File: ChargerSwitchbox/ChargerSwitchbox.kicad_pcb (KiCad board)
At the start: 2 copper layers, 64.1 x 43.2 mm, 13 parts, among them J1 Charger Control, J2 Charger LV, J3 Charger Current Direct, J4 Estop Connector, J5 Charger Current Out, J6 Connector Interlock, U1 PS2501-1, U2 G2RL-1A-E, U3 G2RL-1A-E

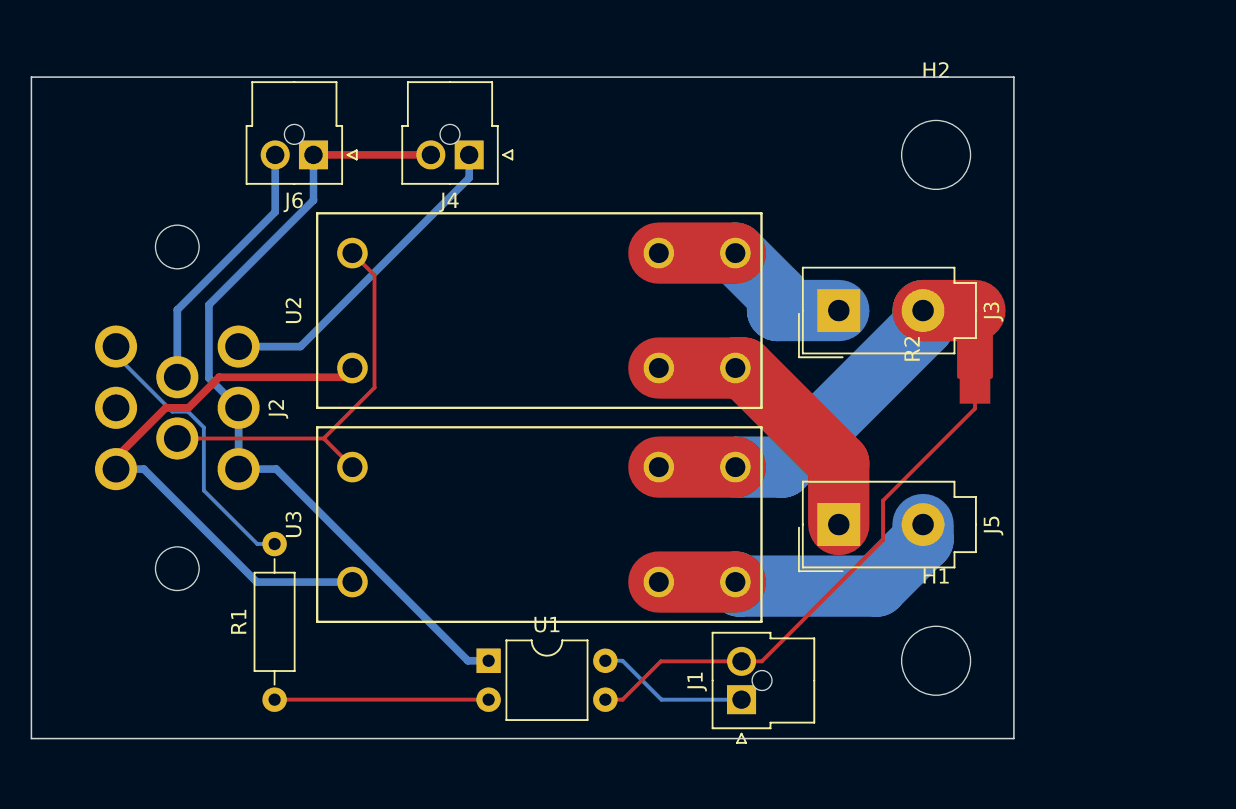
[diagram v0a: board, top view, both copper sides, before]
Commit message: Tweak silkscreen labels on boards for final run
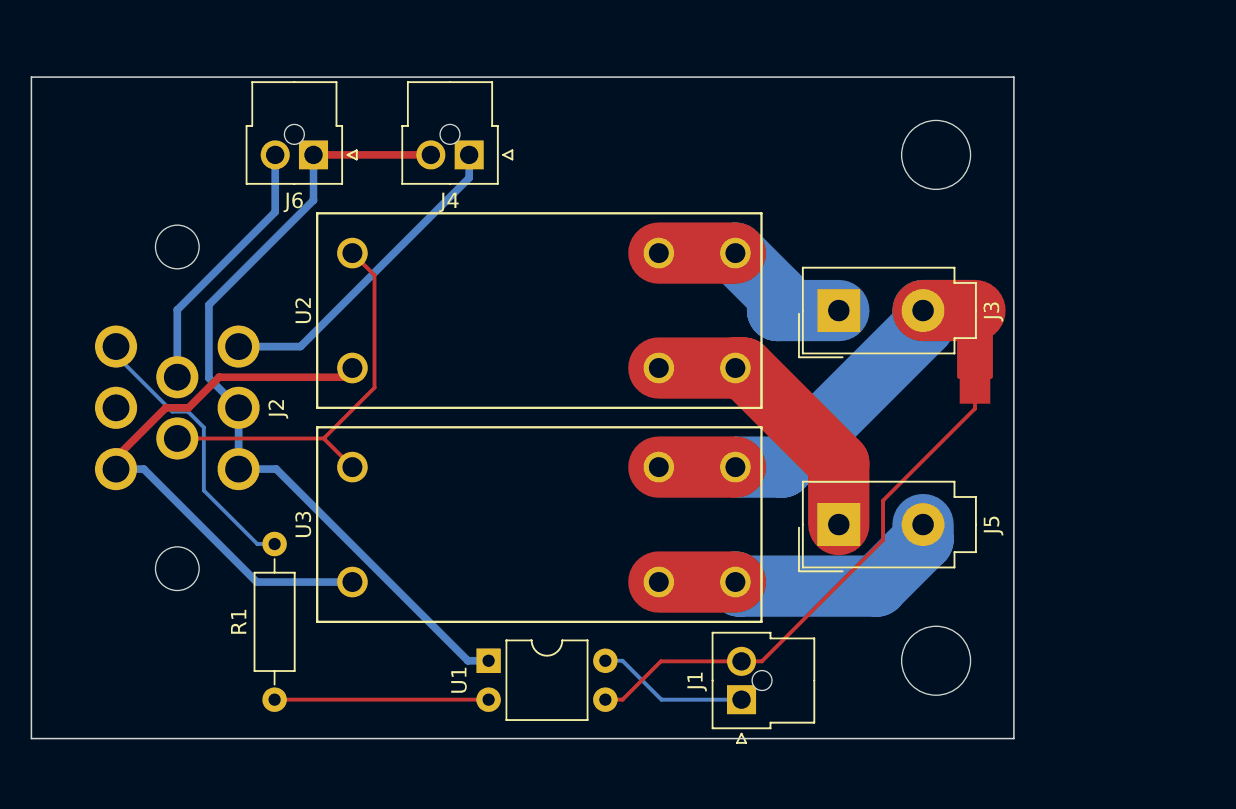
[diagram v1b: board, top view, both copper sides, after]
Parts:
- turned H2 to 180 degrees
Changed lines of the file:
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@@
     (tags "mounting hole 4.5mm no annular")
     (attr virtual)
-    (fp_text reference H1 (at 0 -5.5) (layer F.SilkS)
+    (fp_text reference H1 (at 0 -5.5) (layer F.SilkS) hide
       (effects (font (size 1 1) (thickness 0.15)))
     )
@@
     (descr "Just a \"Net tie\" as an more or less elegant way to connect two different nets without disturbing ERC and DRC.")
     (tags "Just a \"Net tie\" as an more or less elegant way to connect two different nets without disturbing ERC and DRC.")
-    (fp_text reference R2 (at -0.04064 4.06908 270) (layer F.SilkS)
+    (fp_text reference R2 (at 1.905 2.54 270) (layer F.SilkS) hide
       (effects (font (size 1 1) (thickness 0.15)))
     )
@@
     (descr "4-lead though-hole mounted DIP package, row spacing 7.62 mm (300 mils)")
     (tags "THT DIP DIL PDIP 2.54mm 7.62mm 300mil")
-    (fp_text reference U1 (at 3.81 -2.33) (layer F.SilkS)
+    (fp_text reference U1 (at -1.905 1.27 90) (layer F.SilkS)
       (effects (font (size 1 1) (thickness 0.15)))
     )
@@
   (module FSFootprints:G2RL-1A-E (layer F.Cu)
     (at 153.67 43.18)
-    (fp_text reference U2 (at -3.81 0 270) (layer F.SilkS)
+    (fp_text reference U2 (at -3.175 0 270) (layer F.SilkS)
       (effects (font (size 1 1) (thickness 0.15)))
     )
@@
   (module FSFootprints:G2RL-1A-E (layer F.Cu)
     (at 153.67 57.15)
-    (fp_text reference U3 (at -3.81 0 270) (layer F.SilkS)
+    (fp_text reference U3 (at -3.175 0 270) (layer F.SilkS)
       (effects (font (size 1 1) (thickness 0.15)))
     )
@@
   )
   (module Mounting_Holes:MountingHole_4.5mm (layer F.Cu)
-    (at 191.77 33.02)
+    (at 191.77 33.02 180)
     (descr "Mounting Hole 4.5mm, no annular")
     (tags "mounting hole 4.5mm no annular")
     (attr virtual)
-    (fp_text reference H2 (at 0 -5.5) (layer F.SilkS)
+    (fp_text reference H2 (at 0 -5.5 180) (layer F.SilkS) hide
       (effects (font (size 1 1) (thickness 0.15)))
     )
-    (fp_text value MtngHole (at 0 5.5) (layer F.Fab)
+    (fp_text value MtngHole (at 0 5.5 180) (layer F.Fab)
       (effects (font (size 1 1) (thickness 0.15)))
     )
-    (fp_text user %R (at 0.3 0) (layer F.Fab)
+    (fp_text user %R (at 0.3 0 180) (layer F.Fab)
       (effects (font (size 1 1) (thickness 0.15)))
     )
     (fp_circle (center 0 0) (end 4.5 0) (layer Cmts.User) (width 0.15))
     (fp_circle (center 0 0) (end 4.75 0) (layer F.CrtYd) (width 0.05))
-    (pad 1 np_thru_hole circle (at 0 0) (size 4.5 4.5) (drill 4.5) (layers *.Cu *.Mask))
+    (pad 1 np_thru_hole circle (at 0 0 180) (size 4.5 4.5) (drill 4.5) (layers *.Cu *.Mask))
   )
   (module Connectors_Molex:Molex_NanoFit_1x02x2.50mm_Straight (layer F.Cu)

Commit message: Revise boards based on design review
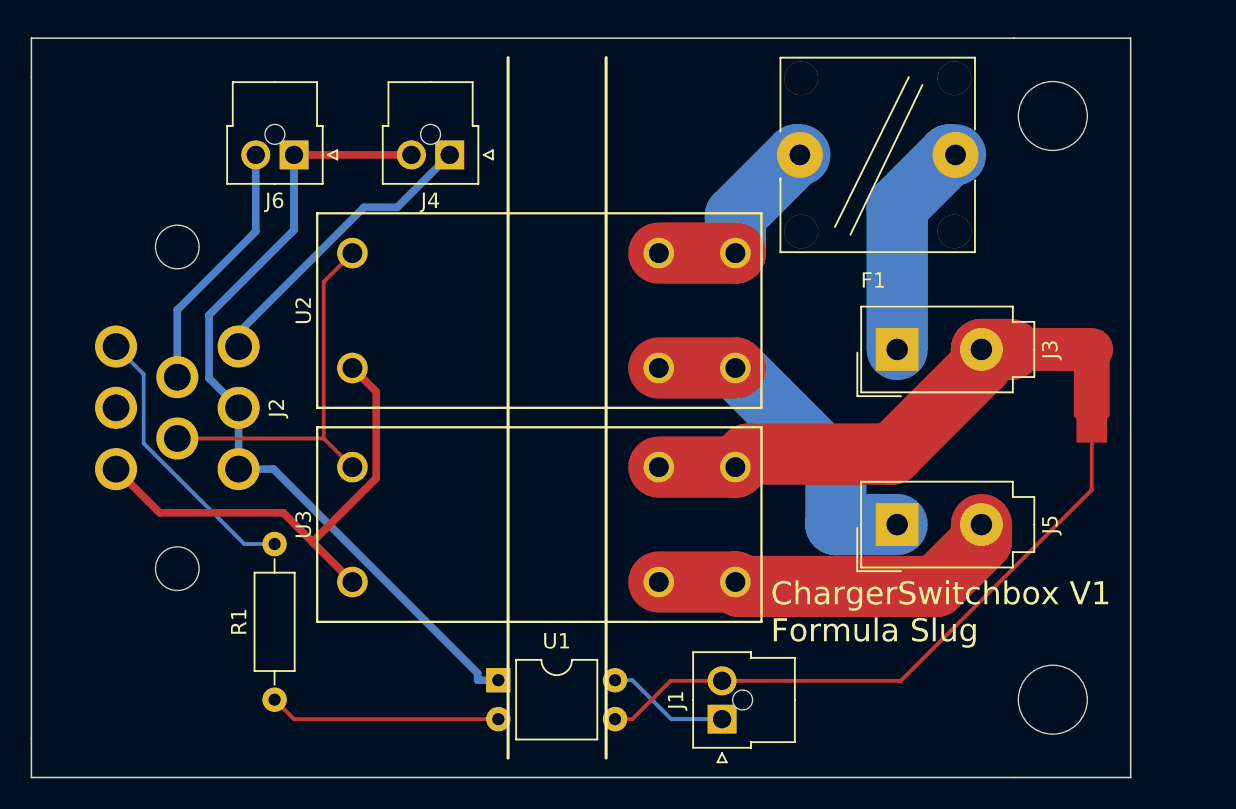
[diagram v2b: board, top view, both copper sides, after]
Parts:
- added F1: Fuse, Fuse_Holders_and_Fuses:Fuseholder5x20_vert_closed_Bulgin_FX0456, F.Cu at (193.0, 33.0)
- R2: footprint Oddities:NetTie-I_Connected_SMD -> FSFootprints:SMDNetTie
- moved R2 8.03 mm to (201.9, 48.3)
- moved H2 8.03 mm to (199.4, 30.5)
- moved H1 8.03 mm to (199.4, 68.6)
- moved J3 4.58 mm to (189.2, 45.7)
- moved J5 3.81 mm to (189.2, 57.1)
- moved J1 1.80 mm to (177.8, 69.8)
- moved U1 1.42 mm to (163.2, 67.3)
- moved J4 1.27 mm to (160.0, 33.0)
- moved J6 1.27 mm to (149.9, 33.0)
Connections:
- U2 pad 3: /CHARGER_OUT+ -> /CHARGER_OUT+_FUSED
- U2 pad 4: /CHARGER_OUT+ -> /CHARGER_OUT+_FUSED
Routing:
- net /CHARGER_OUT+_FUSED: track 0.00 -> 13.3 mm
- net Net-(J1-Pad2): track 34.8 -> 41.4 mm
- net /CHARGER_OUT-: track 25.5 -> 32.0 mm
- net GND: track 37.1 -> 32.2 mm
- net /CHARGER-: track 19.6 -> 23.5 mm
- net /CHARGER+: track 18.3 -> 21.9 mm
- net /CHARGER_TEMP: track 9.94 -> 8.04 mm
- net /12V_SRC: track 21.1 -> 19.5 mm
- net /AIRS_FINAL_CHARGER: track 26.3 -> 25.1 mm
- net Net-(R1-Pad1): track 14.0 -> 15.1 mm
- net +12V: track 53.3 -> 54.2 mm
- net /CHARGER_OUT+: track 13.9 -> 14.5 mm
- net /AIRS_CHARGER_OUT: track 17.2 -> 16.6 mm
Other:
- board size 64.1 x 43.2 mm -> 71.8 x 48.3 mm
- net class ChargerCurrent: via_dia 3.2 -> 6.5; via_drill 2 -> 5
- board text added: "ChargerSwitchbox V1 Formula Slug"

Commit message: add diodes to relay coils among other things
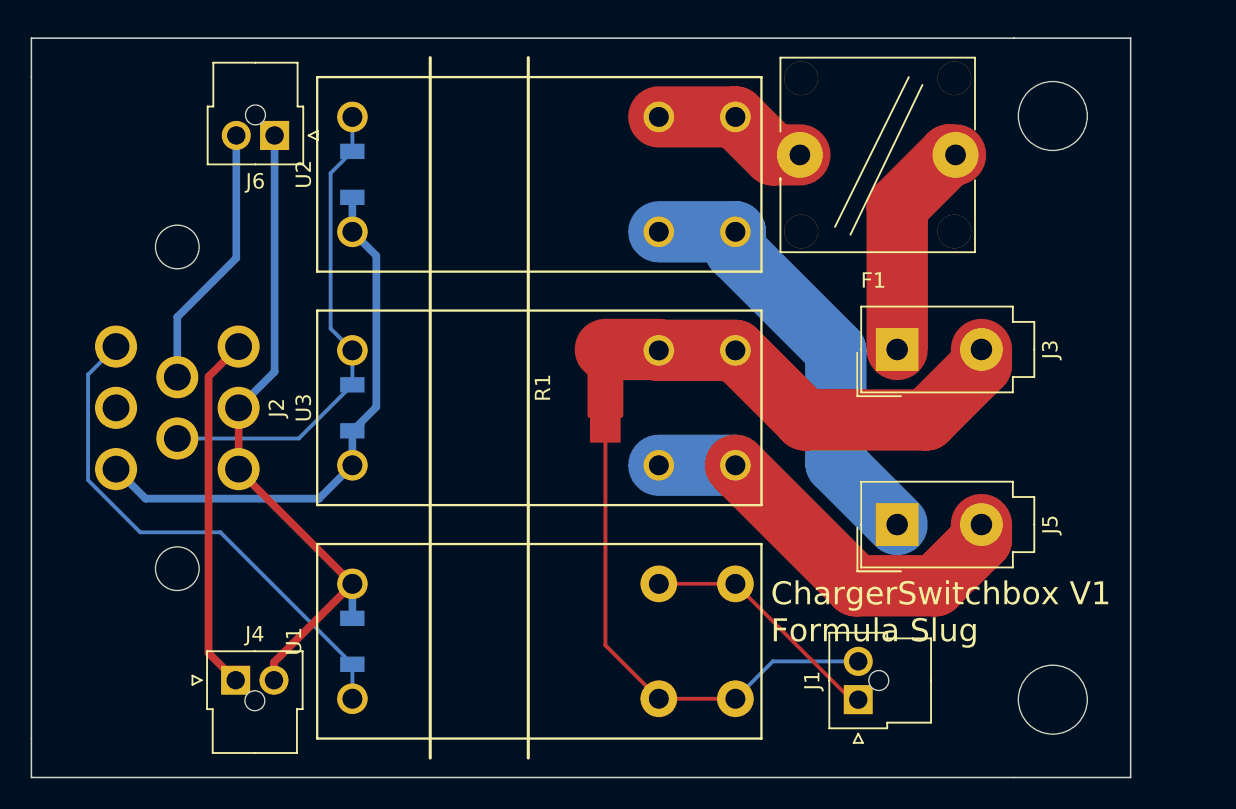
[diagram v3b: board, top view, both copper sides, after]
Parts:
- removed R2: R, FSFootprints:SMDNetTie
- added D1: D, Diodes_SMD:D_1206, B.Cu at (153.7, 64.8)
- added D2: D, Diodes_SMD:D_1206, B.Cu at (153.7, 34.3)
- added D3: D, Diodes_SMD:D_1206, B.Cu at (153.7, 49.5)
- R1: footprint Resistors_THT:R_Axial_DIN0207_L6.3mm_D2.5mm_P10.16mm_Horizontal -> FSFootprints:SMDNetTie
- U1: value PS2501-1 -> G2RL-1A-E; footprint Housings_DIP:DIP-4_W7.62mm -> FSFootprints:G2RL-1A-E
- moved J4 37.0 mm to (146.1, 67.3), turned to 0 degrees
- moved R1 29.6 mm to (170.2, 48.3), turned to 270 degrees
- moved U1 9.86 mm to (153.7, 64.8)
- moved J1 8.98 mm to (186.7, 68.6)
- moved U2 8.89 mm to (153.7, 34.3)
- moved U3 7.62 mm to (153.7, 49.5)
- moved J6 1.80 mm to (148.6, 31.8)
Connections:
- R1 pad 1: Net-(R1-Pad1) -> /CHARGER_OUT-
- R1 pad 2: /CHARGER_CONTROL -> Net-(J1-Pad2)
- U1 pad 3: Net-(J1-Pad2) -> /CHARGER_TEMP
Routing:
- net /CHARGER_CONTROL: track 18.3 -> 34.0 mm
- net Net-(R1-Pad1): track 15.1 -> 0.00 mm
- net +12V: track 54.2 -> 44.0 mm
- net Net-(J1-Pad2): track 41.4 -> 33.2 mm
- net /CHARGER_TEMP: track 8.04 -> 16.2 mm
- net /CHARGER+: track 21.9 -> 28.5 mm
- net /AIRS_FINAL_CHARGER: track 25.1 -> 31.6 mm
- net /12V_SRC: track 19.5 -> 23.3 mm
- net GND: track 32.2 -> 35.9 mm
- net /CHARGER-: track 23.5 -> 26.5 mm
- net /CHARGER_OUT-: track 32.0 -> 29.0 mm
- net /CHARGER_OUT+_FUSED: track 13.3 -> 10.2 mm
- net /AIRS_CHARGER_OUT: track 16.6 -> 17.4 mm

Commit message: hopefully finalize PCBs for send to manufacturing
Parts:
- F1: footprint Fuse_Holders_and_Fuses:Fuseholder5x20_vert_closed_Bulgin_FX0456 -> FSFootprints:Fuseholder5x20_vert
- moved R1 31.7 mm to (200.7, 57.1)
- moved J5 14.0 mm to (189.2, 43.2)
- moved J3 8.89 mm to (189.2, 54.6)
- moved D1 2.54 mm to (153.7, 67.3)
- moved U1 2.54 mm to (153.7, 67.3)
- moved F1 2.29 mm to (191.8, 34.9), turned to 135 degrees
- moved D2 1.91 mm to (153.7, 36.2)
- moved U2 1.91 mm to (153.7, 36.2)
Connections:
- U1 pad 4: /CHARGER_TEMP -> Net-(J1-Pad2)
- U1 pad 6: Net-(J1-Pad2) -> /CHARGER_TEMP
- U2 pad 4: /CHARGER_OUT+_FUSED -> /CHARGER+
- U2 pad 6: /CHARGER+ -> /CHARGER_OUT+_FUSED
- U3 pad 4: /CHARGER_OUT- -> /CHARGER-
- U3 pad 6: /CHARGER- -> /CHARGER_OUT-
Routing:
- net /CHARGER_OUT+: track 14.5 -> 36.5 mm
- net /CHARGER_OUT-: track 29.0 -> 44.4 mm
- net /CHARGER_OUT+_FUSED: track 10.2 -> 22.5 mm
- net /CHARGER+: track 28.5 -> 19.4 mm
- net /CHARGER_TEMP: track 16.2 -> 20.5 mm
- net GND: track 35.9 -> 39.5 mm
- net /CHARGER_CONTROL: track 34.0 -> 31.9 mm
- net /CHARGER-: track 26.5 -> 28.5 mm
- net /AIRS_FINAL_CHARGER: track 31.6 -> 29.6 mm
- net Net-(J1-Pad2): track 33.2 -> 32.1 mm
- net +12V: track 44.0 -> 44.8 mm

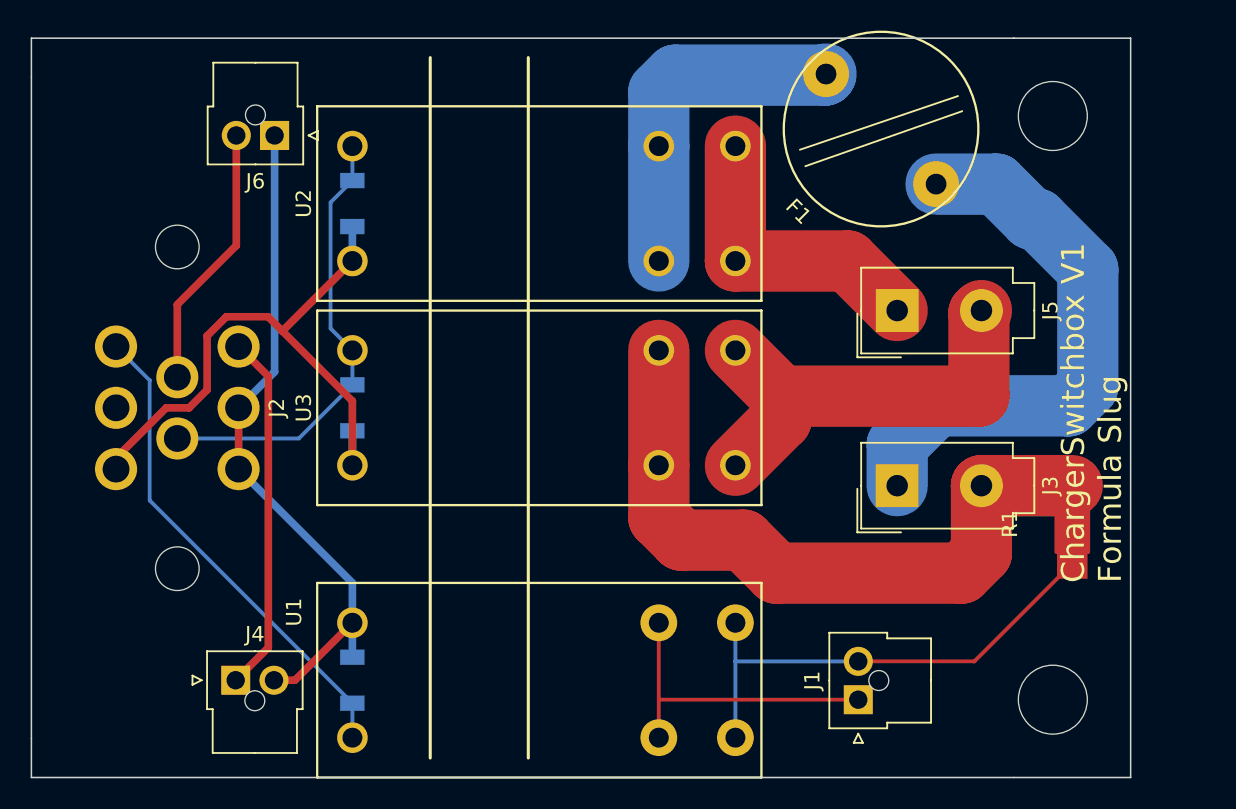
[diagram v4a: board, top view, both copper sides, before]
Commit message: Edit some component labels and other items for PCB send out
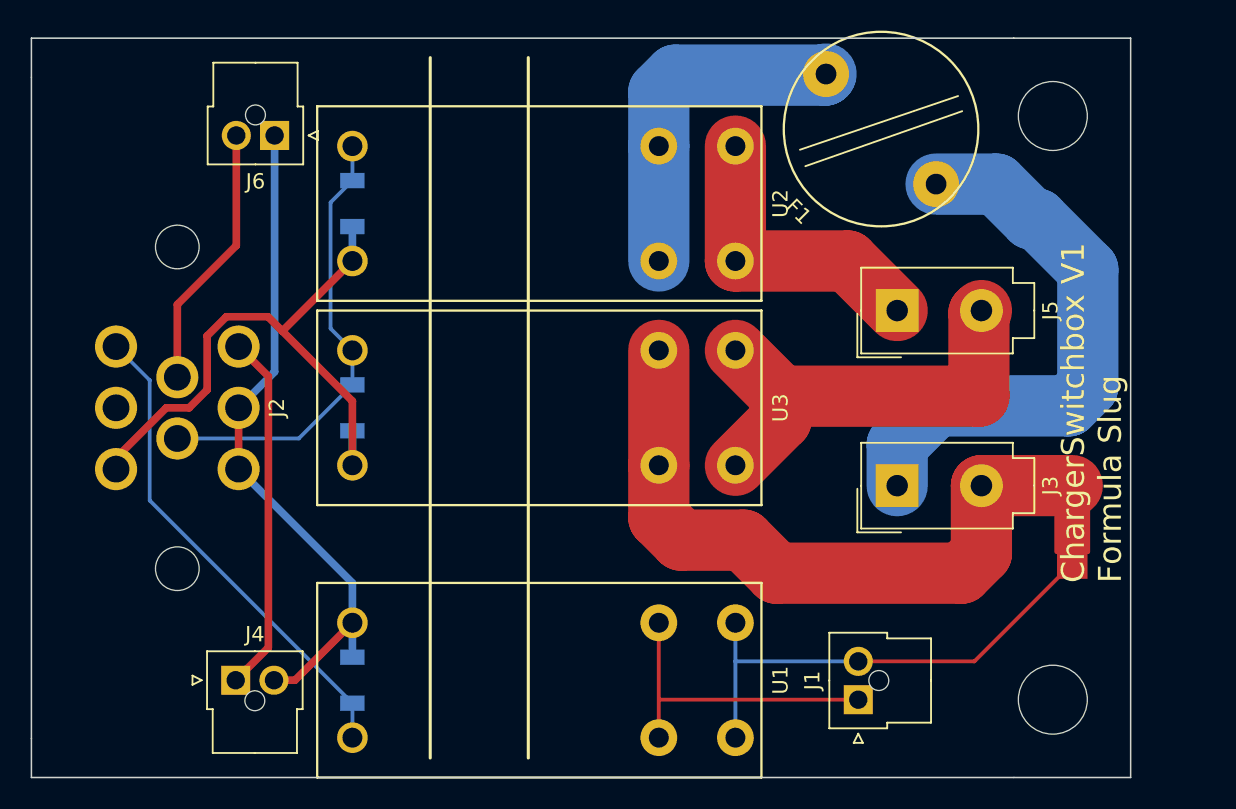
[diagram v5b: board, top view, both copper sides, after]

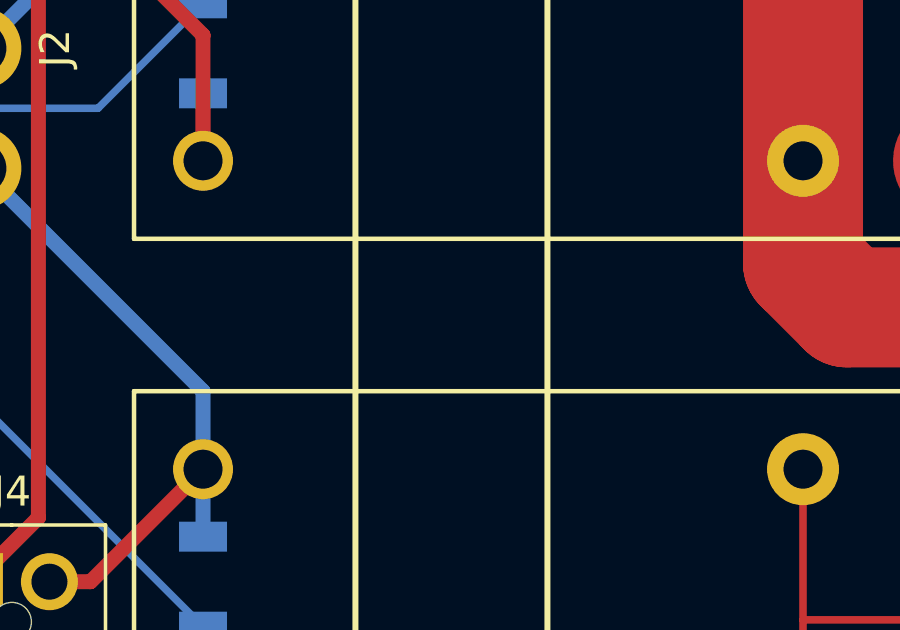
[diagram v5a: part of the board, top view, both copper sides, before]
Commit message: add TS/GLV labels to Charger Switchbox pcb
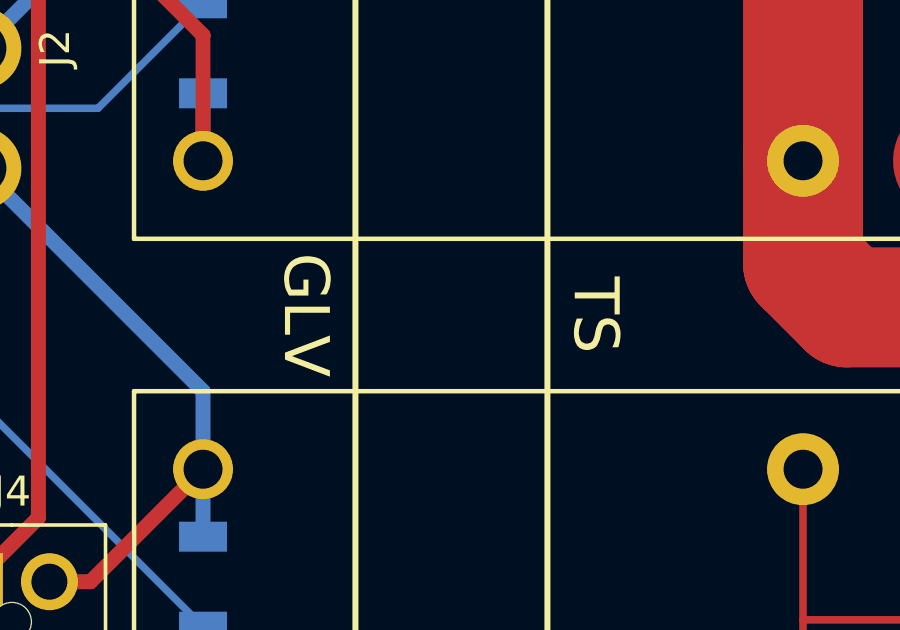
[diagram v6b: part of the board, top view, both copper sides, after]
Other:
- board text added: "TS GLV"
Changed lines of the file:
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@@
     (area 132.064999 23.584553 205.183 75.555)
     (thickness 1.6)
-    (drawings 11)
+    (drawings 13)
     (tracks 82)
     (zones 0)
@@
       (net 3 /AIRS_FINAL_CHARGER))
   )
+  (gr_text "TS\n\n\n\nGLV" (at 161.925 58.42 270) (layer B.SilkS)
+    (effects (font (size 1.5 1.5) (thickness 0.3)) (justify mirror))
+  )
+  (gr_text "TS\n\n\n\nGLV" (at 161.925 58.42 270) (layer F.SilkS)
+    (effects (font (size 1.5 1.5) (thickness 0.3)))
+  )
   (gr_text "ChargerSwitchbox V1\nFormula Slug" (at 201.93 60.96 90) (layer F.SilkS)
